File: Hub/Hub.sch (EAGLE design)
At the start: 9 parts

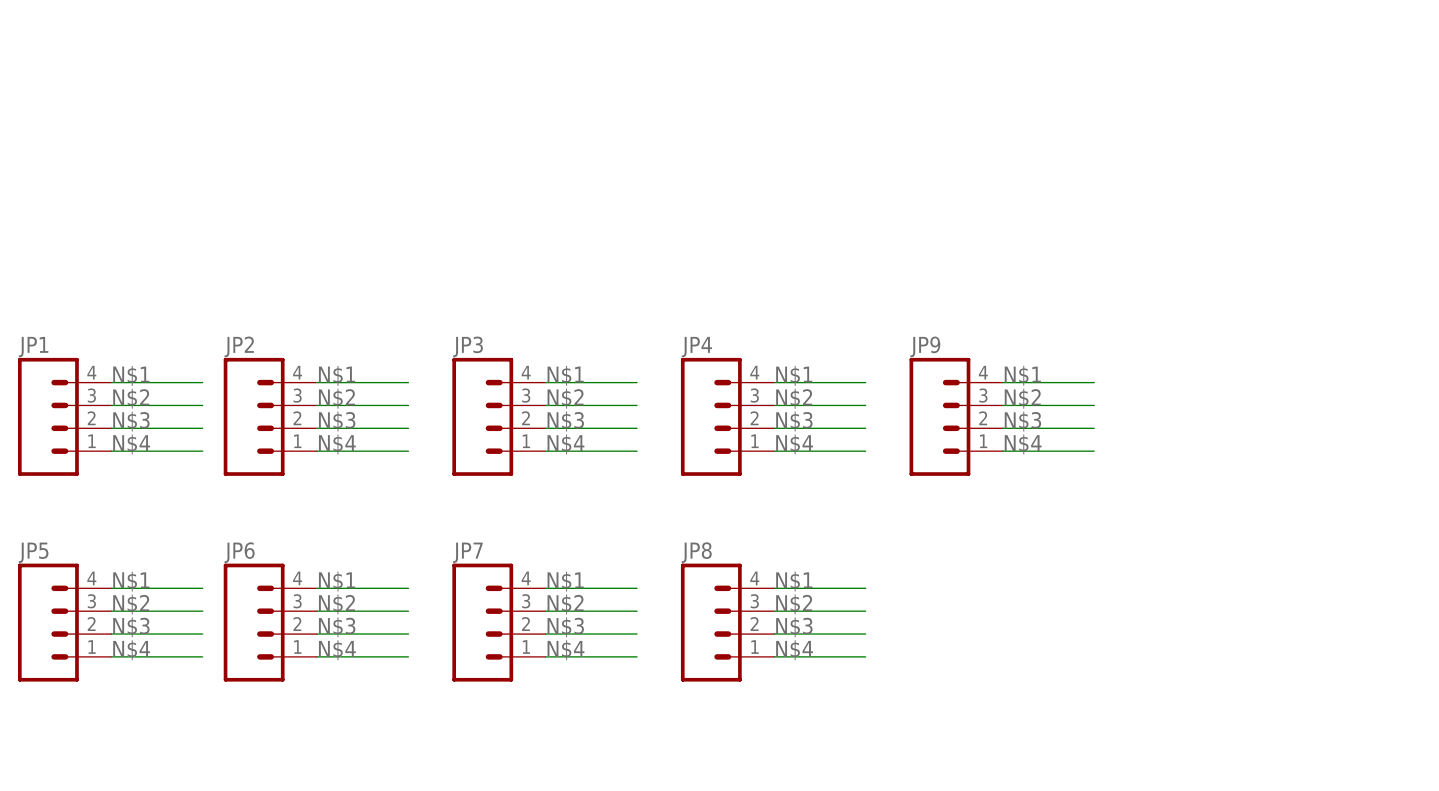
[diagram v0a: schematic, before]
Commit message: Cleaned up pcb repository file structure.
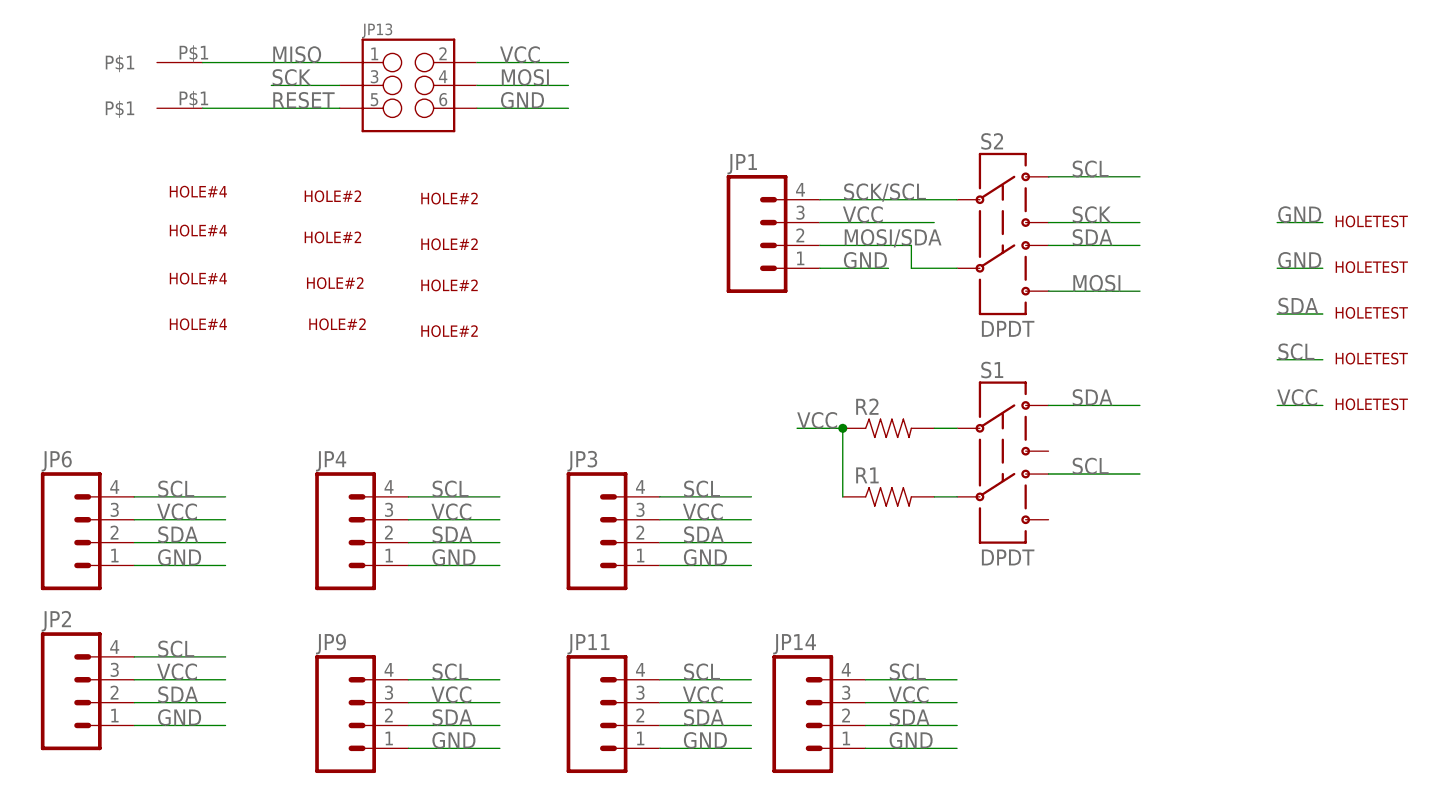
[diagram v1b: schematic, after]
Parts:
- removed JP5, JP7, JP8: (no value), SparkFun-Connectors:M041X04_NO_SILK
- added JP11, JP14: (no value), SparkFun-Connectors:M04LOCK
- added JP13: (no value), SparkFun-Connectors:M03X2SHROUD
- added R1, R2: (no value), SparkFun-Resistors:RESISTOR0805-RES
- added S1, S2: DPDT, SparkFun-Electromechanical:SWITCH-DPDTAYZ0202
- added U$1, U$2: SPRING-CONNECTOR, IntegerLabs:SPRING-CONNECTOR
- added U$10, U$11, U$12, U$13, U$14, U$7, U$8, U$9: HOLE#2, IntegerLabs:HOLE#2
- added U$15, U$16, U$17, U$18, U$19: HOLETEST, IntegerLabs:HOLETEST
- added U$3, U$4, U$5, U$6: HOLE#4, IntegerLabs:HOLE#4
- JP1, JP4: device SparkFun-Connectors:M041X04_NO_SILK -> SparkFun-Connectors:M04LOCK
- JP2, JP3, JP6, JP9: device SparkFun-Connectors:M041X04_NO_SILK -> SparkFun-Connectors:M04POLAR_LOCK
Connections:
- removed net N$1: JP1.4, JP2.4, JP3.4, JP4.4, JP5.4, JP6.4, JP7.4, JP8.4, JP9.4
- removed net N$2: JP1.3, JP2.3, JP3.3, JP4.3, JP5.3, JP6.3, JP7.3, JP8.3, JP9.3
- new net GND: JP1.1, JP11.1, JP13.6, JP14.1, JP2.1, JP3.1, JP4.1, JP6.1, JP9.1, U$15.HOLE, U$16.HOLE
- new net MISO: JP13.1, U$1.P$1
- new net MOSI: JP13.4, S2.6
- new net MOSI/SDA: JP1.2, S2.5
- new net RESET: JP13.5, U$2.P$1
- new net SCK: JP13.3, S2.3
- new net SCK/SCL: JP1.4, S2.2
- new net SCL: JP11.4, JP14.4, JP2.4, JP3.4, JP4.4, JP6.4, JP9.4, S1.4, S2.1, U$18.HOLE
- new net SDA: JP11.2, JP14.2, JP2.2, JP3.2, JP4.2, JP6.2, JP9.2, S1.1, S2.4, U$17.HOLE
- new net VCC: JP1.3, JP11.3, JP13.2, JP14.3, JP2.3, JP3.3, JP4.3, JP6.3, JP9.3, R1.1, R2.1, U$19.HOLE
- net N$3: now also R1.2, S1.5; no longer JP1.2, JP2.2, JP3.2, JP4.2, JP5.2, JP6.2, JP7.2, JP8.2, JP9.2
- net N$4: now also R2.2, S1.2; no longer JP1.1, JP2.1, JP3.1, JP4.1, JP5.1, JP6.1, JP7.1, JP8.1, JP9.1
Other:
- moved on the sheet: JP1, JP2, JP3, JP4, JP6, JP9

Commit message: Latest version of schematics and boards
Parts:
- removed JP13: (no value), SparkFun-Connectors:M03X2SHROUD
- removed JP9: (no value), SparkFun-Connectors:M04POLAR_LOCK
- removed S1, S2: DPDT, SparkFun-Electromechanical:SWITCH-DPDTAYZ0202
- added C6: 10uF, SparkFun-Capacitors:10UF-20V-10%(TANT)
- added F1: PTCSMD, SparkFun-PowerIC:PTCSMD
- added ICSP: (no value), SparkFun-Connectors:M03X22X3_SILK_SM
- added JP5: M023.5MM_LOCK, SparkFun-Connectors:M023.5MM_LOCK
- added LED1: (no value), led:LEDCHIPLED_0805
- added Q1, Q2, Q5: BSS138, SparkFun-DiscreteSemi:MOSFET-NCHANNELBSS138
- added Q3, Q4: IRLML5203, transistor-power:IRLML5203
- added Q6: TRANSISTOR-DUAL-PNP, IntegerLabs:TRANSISTOR-DUAL-PNP
- added Q7: SI2333DDS-T1-GE3, SparkFun-DiscreteSemi:MOSFET-PCHANNELSMD
- added R3, R4: 2k, SparkFun-Passives:RESISTOR0805-RES
- added R5, R6: (no value), SparkFun-Resistors:RESISTOR0805-RES
- added R7, R8, R9: 2k, SparkFun-Resistors:RESISTOR0805-RES
- added SJ1: SOLDERJUMPERNO, SparkFun-Passives:SOLDERJUMPERNO
- added U$21: DC-JACK, IntegerLabs:DC-JACK
- added U$22, U$23, U$24: SPRING-CONNECTOR, IntegerLabs:SPRING-CONNECTOR
- added U$25, U$26, U$27: HOLE#2, IntegerLabs:HOLE#2
- added U$28: HEADER-1X6MOLEX-KK254, IntegerLabs:HEADER-1X6MOLEX-KK254
- JP2, JP3, JP6: value (none) -> HEADER-1X4MOLEX-SL; device SparkFun-Connectors:M04POLAR_LOCK -> IntegerLabs:HEADER-1X4MOLEX-SL
- R1: value (none) -> 2k
- R2: value (none) -> 390; device SparkFun-Resistors:RESISTOR0805-RES -> SparkFun-Passives:RESISTOR0805-RES
- U$15: value HOLETEST -> HOLE#2; device IntegerLabs:HOLETEST -> IntegerLabs:HOLE#2
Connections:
- removed net MOSI/SDA: JP1.2, S2.5
- removed net SCK/SCL: JP1.4, S2.2
- new net +3.3V: Q1.G, Q2.G, R3.2, R4.2, U$28.P3
- new net N$1: Q3.G, Q4.G, Q5.D, R9.1, SJ1.2
- new net N$2: F1.1, JP5.2, U$21.P$1
- new net N$5: F1.2, Q6A.E, Q7.D
- new net N$6: Q3.D, R7.1
- new net N$7: Q4.D, R8.1
- new net N$8: LED1.A, R2.1
- new net PU_EN: Q5.G, R1.2, U$28.P6
- new net SCL3.3: Q1.S, R3.1, U$28.P4
- new net SDA3.3: Q2.S, R4.1, U$28.P2
- new net VPROG: ICSP.2, U$24.P$1
- net GND: now also C6.-, ICSP.6, JP5.1, LED1.C, Q5.S, R1.1, R5.2, R6.1, SJ1.1, U$21.P$2, U$28.P1; no longer JP13.6, JP9.1, U$15.HOLE
- net MISO: now also ICSP.1; no longer JP13.1
- net MOSI: now also ICSP.4, U$23.P$1; no longer JP13.4, S2.6
- net N$3: now also Q6A.B, Q6A.C, Q6B.B, Q7.G, R5.1; no longer R1.2, S1.5
- net N$4: now also Q6B.C, R6.2; no longer R2.2, S1.2
- net RESET: now also ICSP.5; no longer JP13.5
- net SCK: now also ICSP.3, U$22.P$1; no longer JP13.3, S2.3
- net SCL: now also JP1.4, Q1.D, R8.2; no longer JP9.4, S1.4, S2.1
- net SDA: now also JP1.2, Q2.D, R7.2; no longer JP9.2, S1.1, S2.4
- net VCC: now also C6.+, Q3.S, Q4.S, Q6B.E, Q7.S, R2.2, R9.2, U$28.P5; no longer JP13.2, JP9.3, R1.1, R2.1
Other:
- moved on the sheet: JP1, JP11, JP14, JP4, R1, R2

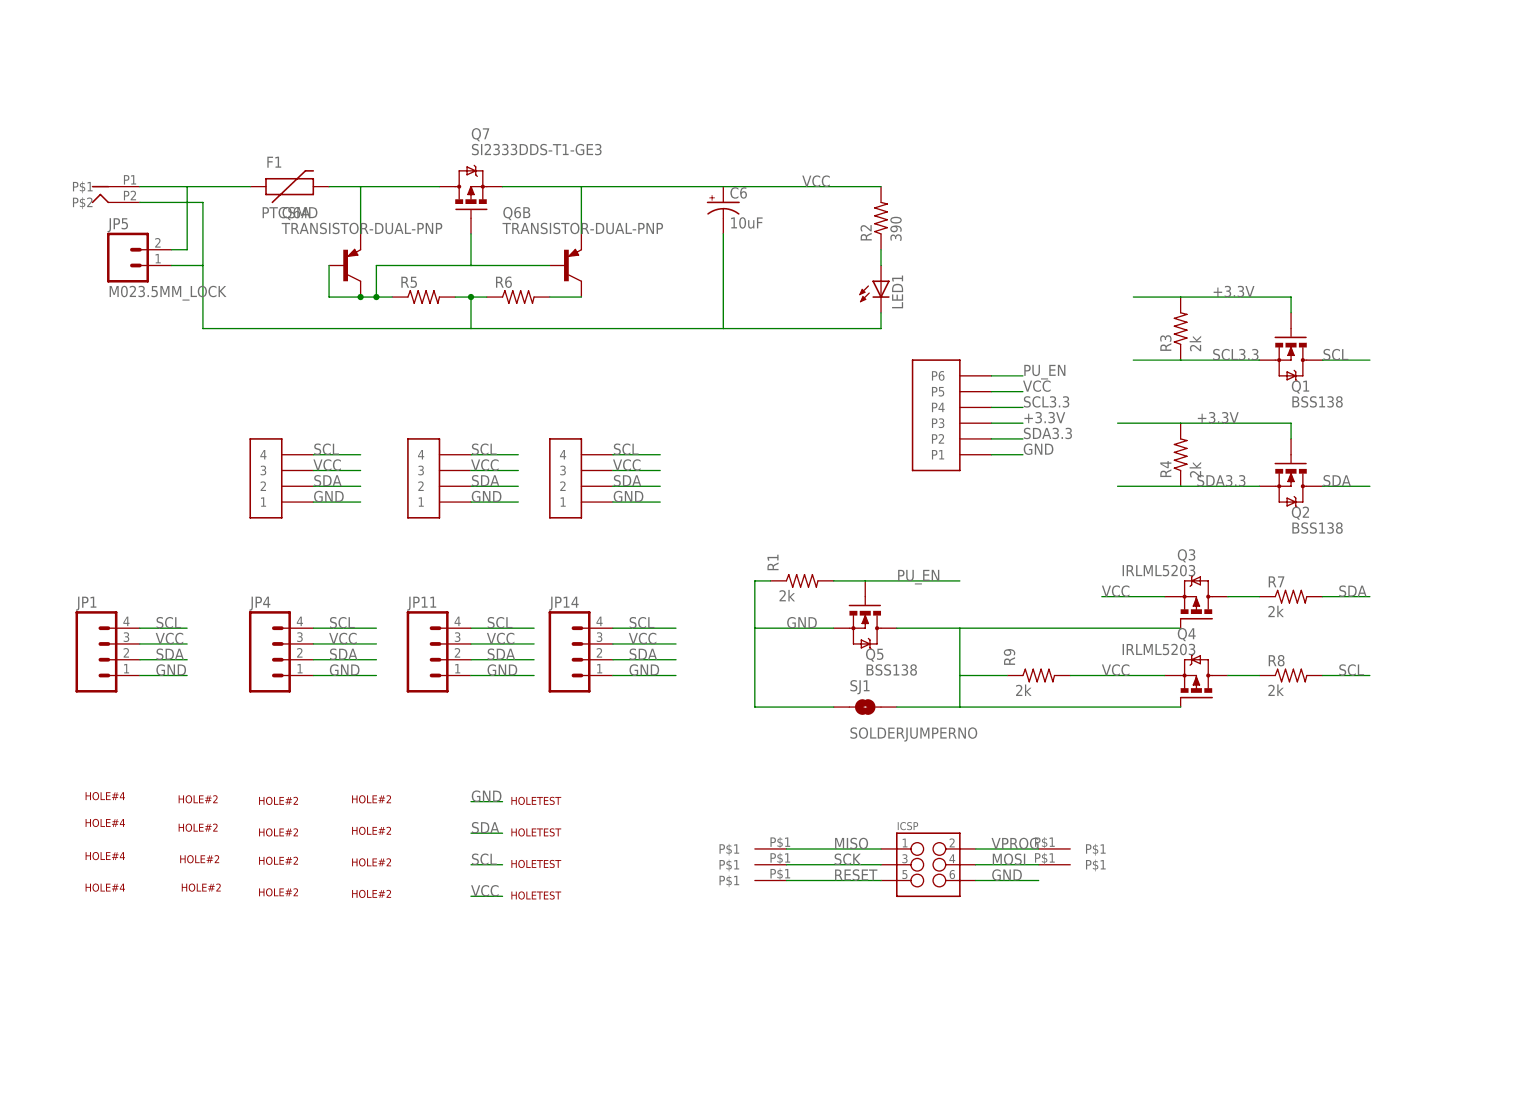
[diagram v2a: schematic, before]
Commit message: New Hub with smaller form factor and bus connectors on bottom.
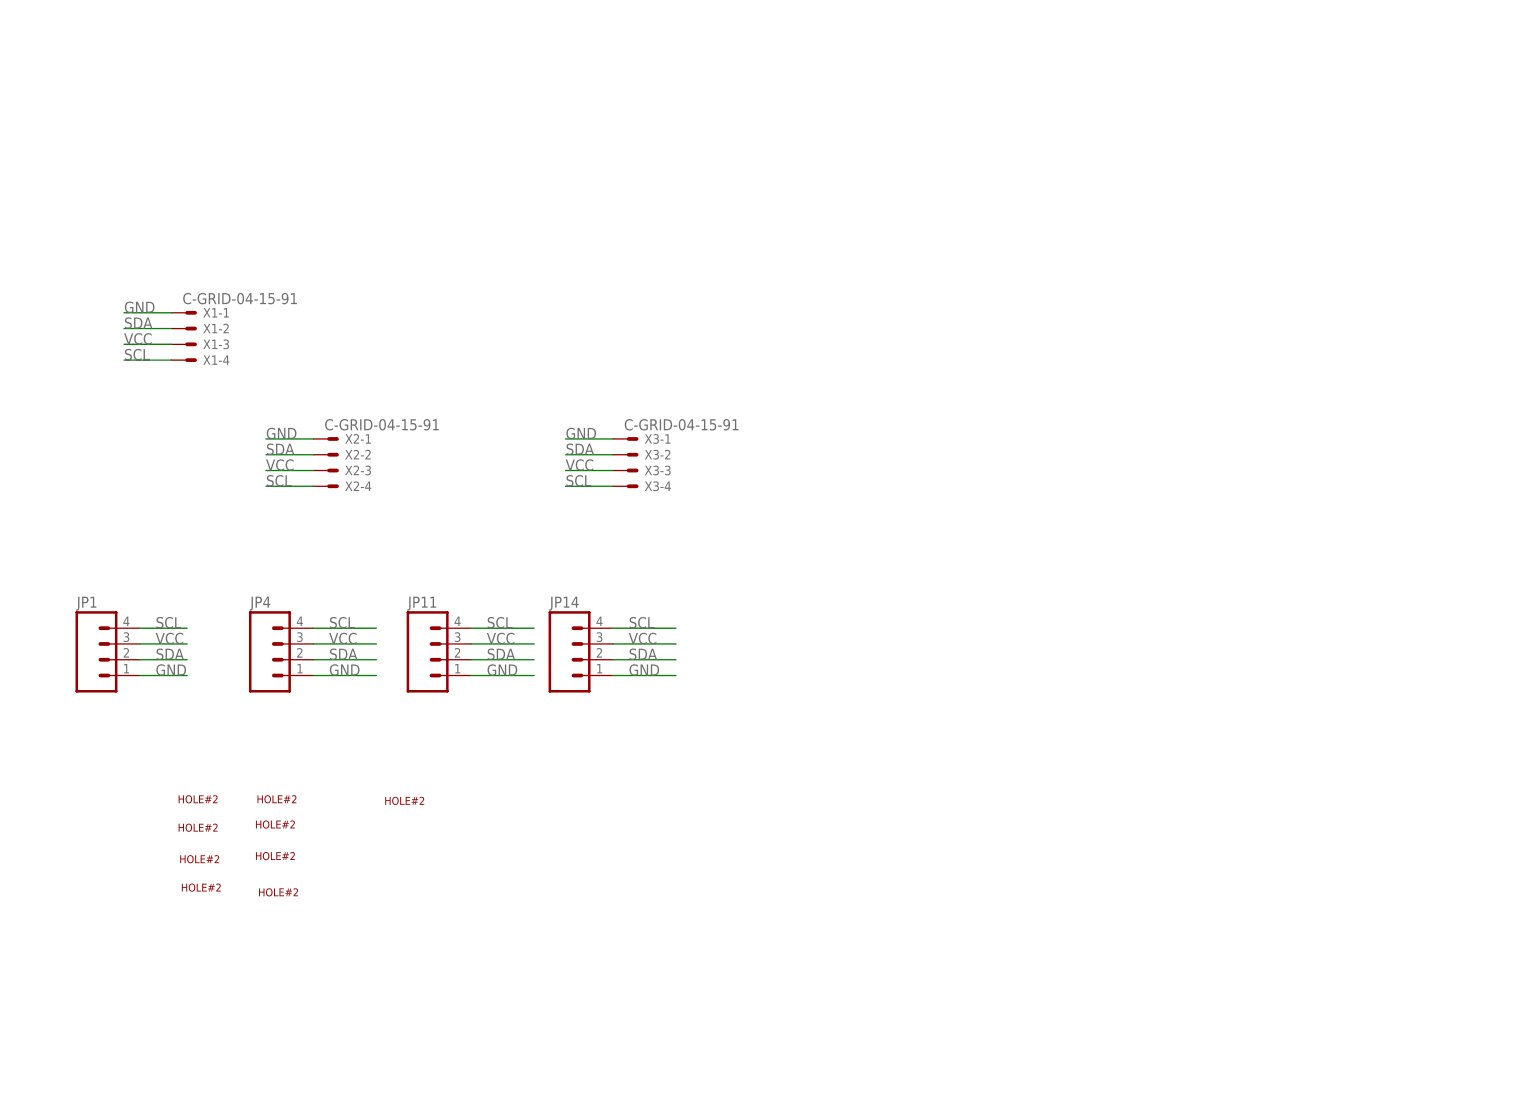
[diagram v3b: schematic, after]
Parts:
- removed C6: 10uF, SparkFun-Capacitors:10UF-20V-10%(TANT)
- removed F1: PTCSMD, SparkFun-PowerIC:PTCSMD
- removed ICSP: (no value), SparkFun-Connectors:M03X22X3_SILK_SM
- removed JP2, JP3, JP6: HEADER-1X4MOLEX-SL, IntegerLabs:HEADER-1X4MOLEX-SL
- removed JP5: M023.5MM_LOCK, SparkFun-Connectors:M023.5MM_LOCK
- removed LED1: (no value), led:LEDCHIPLED_0805
- removed Q1, Q2, Q5: BSS138, SparkFun-DiscreteSemi:MOSFET-NCHANNELBSS138
- removed Q3, Q4: IRLML5203, transistor-power:IRLML5203
- removed Q6: TRANSISTOR-DUAL-PNP, IntegerLabs:TRANSISTOR-DUAL-PNP
- removed Q7: SI2333DDS-T1-GE3, SparkFun-DiscreteSemi:MOSFET-PCHANNELSMD
- removed R1, R7, R8, R9: 2k, SparkFun-Resistors:RESISTOR0805-RES
- removed R2: 390, SparkFun-Passives:RESISTOR0805-RES
- removed R3, R4: 2k, SparkFun-Passives:RESISTOR0805-RES
- removed R5, R6: (no value), SparkFun-Resistors:RESISTOR0805-RES
- removed SJ1: SOLDERJUMPERNO, SparkFun-Passives:SOLDERJUMPERNO
- removed U$1, U$2, U$22, U$23, U$24: SPRING-CONNECTOR, IntegerLabs:SPRING-CONNECTOR
- removed U$15, U$25, U$26, U$27: HOLE#2, IntegerLabs:HOLE#2
- removed U$16, U$17, U$18, U$19: HOLETEST, IntegerLabs:HOLETEST
- removed U$21: DC-JACK, IntegerLabs:DC-JACK
- removed U$28: HEADER-1X6MOLEX-KK254, IntegerLabs:HEADER-1X6MOLEX-KK254
- removed U$3, U$4, U$5: HOLE#4, IntegerLabs:HOLE#4
- added X1, X2, X3: C-GRID-04-15-91, con-molex:C-GRID-04-15-91
- U$6: value HOLE#4 -> HOLE#2; device IntegerLabs:HOLE#4 -> IntegerLabs:HOLE#2
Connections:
- removed net +3.3V: Q1.G, Q2.G, R3.2, R4.2, U$28.P3
- removed net MISO: ICSP.1, U$1.P$1
- removed net MOSI: ICSP.4, U$23.P$1
- removed net N$1: Q3.G, Q4.G, Q5.D, R9.1, SJ1.2
- removed net N$2: F1.1, JP5.2, U$21.P$1
- removed net N$3: Q6A.B, Q6A.C, Q6B.B, Q7.G, R5.1
- removed net N$4: Q6B.C, R6.2
- removed net N$5: F1.2, Q6A.E, Q7.D
- removed net N$6: Q3.D, R7.1
- removed net N$7: Q4.D, R8.1
- removed net N$8: LED1.A, R2.1
- removed net PU_EN: Q5.G, R1.2, U$28.P6
- removed net RESET: ICSP.5, U$2.P$1
- removed net SCK: ICSP.3, U$22.P$1
- removed net SCL3.3: Q1.S, R3.1, U$28.P4
- removed net SDA3.3: Q2.S, R4.1, U$28.P2
- removed net VPROG: ICSP.2, U$24.P$1
- net GND: now also X1-1.S, X2-1.S, X3-1.S; no longer C6.-, ICSP.6, JP2.1, JP3.1, JP5.1, JP6.1, LED1.C, Q5.S, R1.1, R5.2, R6.1, SJ1.1, U$16.HOLE, U$21.P$2, U$28.P1
- net SCL: now also X1-4.S, X2-4.S, X3-4.S; no longer JP2.4, JP3.4, JP6.4, Q1.D, R8.2, U$18.HOLE
- net SDA: now also X1-2.S, X2-2.S, X3-2.S; no longer JP2.2, JP3.2, JP6.2, Q2.D, R7.2, U$17.HOLE
- net VCC: now also X1-3.S, X2-3.S, X3-3.S; no longer C6.+, JP2.3, JP3.3, JP6.3, Q3.S, Q4.S, Q6B.E, Q7.S, R2.2, R9.2, U$19.HOLE, U$28.P5

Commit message: various minor changes
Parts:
- added JP2, JP3, JP5, JP6, JP7, JP8: (no value), SparkFun-Connectors:M04LOCK
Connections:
- net GND: now also JP2.1, JP3.1, JP5.1, JP6.1, JP7.1, JP8.1
- net SCL: now also JP2.4, JP3.4, JP5.4, JP6.4, JP7.4, JP8.4
- net SDA: now also JP2.2, JP3.2, JP5.2, JP6.2, JP7.2, JP8.2
- net VCC: now also JP2.3, JP3.3, JP5.3, JP6.3, JP7.3, JP8.3
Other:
- moved on the sheet: X1-1, X1-2, X1-3, X1-4, X2-1, X2-2, X2-3, X2-4, X3-1, X3-2, X3-3, X3-4

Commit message: Checkpointing PCB designs
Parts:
- added C1, C2, C3, C4: 68uF, SparkFun-Capacitors:CAP1210
- added F1: (no value), SparkFun-Passives:RESISTOR0805-RES
- added LED1: (no value), adafruit:LEDCHIP-LED0805
- added Q2: DMMT5401, IntegerLabs:TRANSISTOR-DUAL-PNP
- added Q3: DMG2305UX, transistor-power:IRLML5203
- added R2: 680, SparkFun-Passives:RESISTOR0805-RES
- added R5: 10k 1%, SparkFun-Passives:RESISTOR0805-RES
- added R9: 47k 1%, SparkFun-Passives:RESISTOR0805-RES
- added U$1: DC-JACKLOWPRO, IntegerLabs:DC-JACKLOWPRO
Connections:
- new net N$1: F1.2, U$1.P$1
- new net N$14: Q2A.B, Q2A.C, Q2B.B, R5.2
- new net N$16: Q2B.C, Q3.G, R9.2
- new net N$8: LED1.A, R2.1
- new net VREG: F1.1, Q2A.E, Q3.D
- net GND: now also C1.2, C2.2, C3.2, C4.2, LED1.C, R5.1, R9.1, U$1.P$2
- net VCC: now also C1.1, C2.1, C3.1, C4.1, Q2B.E, Q3.S, R2.2
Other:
- note added: "GRM32ER60J476ME20L"
